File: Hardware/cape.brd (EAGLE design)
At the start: 87 x 118 mm, 67 parts, among them IC1 RT7258, IC2 RT7258, J1 JST-BM07B-GHS-TBT, J10 JST-BM07B-GHS-TBT, J11 JST-BM07B-GHS-TBT, J12 JST-BM07B-GHS-TBT, J13 JST-BM07B-GHS-TBT, J14 JST-BM07B-GHS-TBT, J15 JST-BM07B-GHS-TBT, J16 JST-BM07B-GHS-TBT, J17 JST-BM07B-GHS-TBT, J18 JST-BM07B-GHS-TBT, J19 JST-BM07B-GHS-TBT, J2 JST-BM07B-GHS-TBT, J20 JST-BM07B-GHS-TBT, J21 JST-BM07B-GHS-TBT, J22 JST-BM07B-GHS-TBT, J23 JST-BM07B-GHS-TBT, J24 JST-BM07B-GHS-TBT, J25 JST-BM07B-GHS-TBT, J26 JST-BM07B-GHS-TBT, J27 JST-BM07B-GHS-TBT, J28 JST-BM07B-GHS-TBT, J29 JST-BM07B-GHS-TBT, J3 JST-BM07B-GHS-TBT, J30 JST-BM07B-GHS-TBT, J31 JST-BM07B-GHS-TBT, J32 JST-BM07B-GHS-TBT, J4 JST-BM07B-GHS-TBT, J5 JST-BM07B-GHS-TBT, J6 JST-BM07B-GHS-TBT, J7 JST-BM07B-GHS-TBT, J8 JST-BM07B-GHS-TBT, J9 JST-BM07B-GHS-TBT, Q1 FDS6670, Q2 FDS6670, X1 RJ45-6L2-B, X2 RJ45-6L2-B

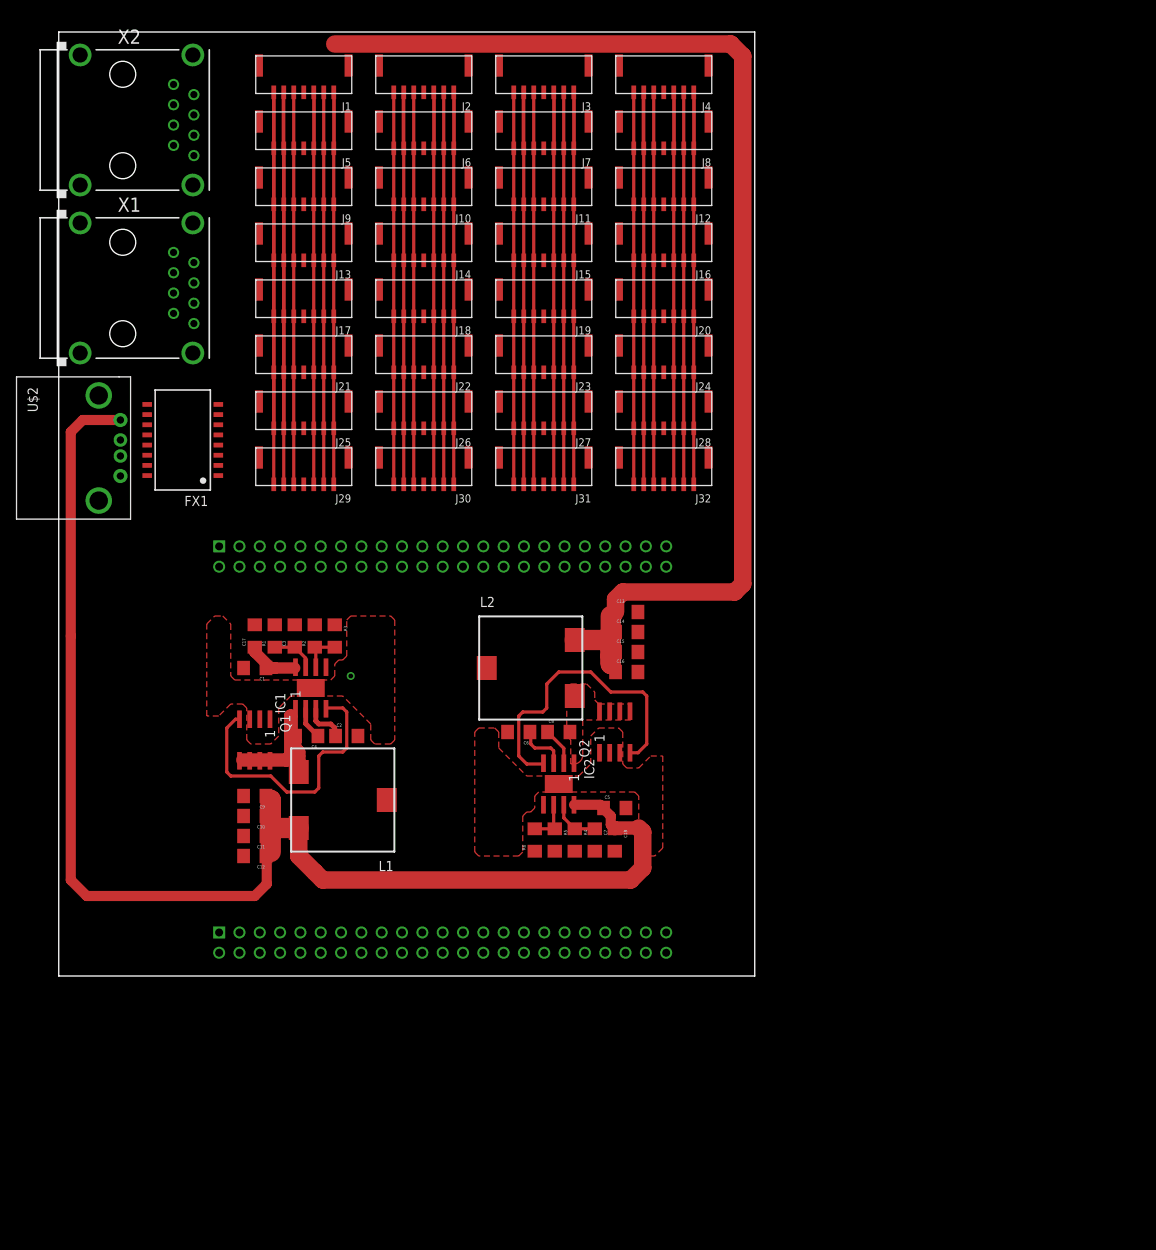
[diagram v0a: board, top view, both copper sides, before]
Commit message: added circuits to control backlights, but I'm going to pull them out for this revision
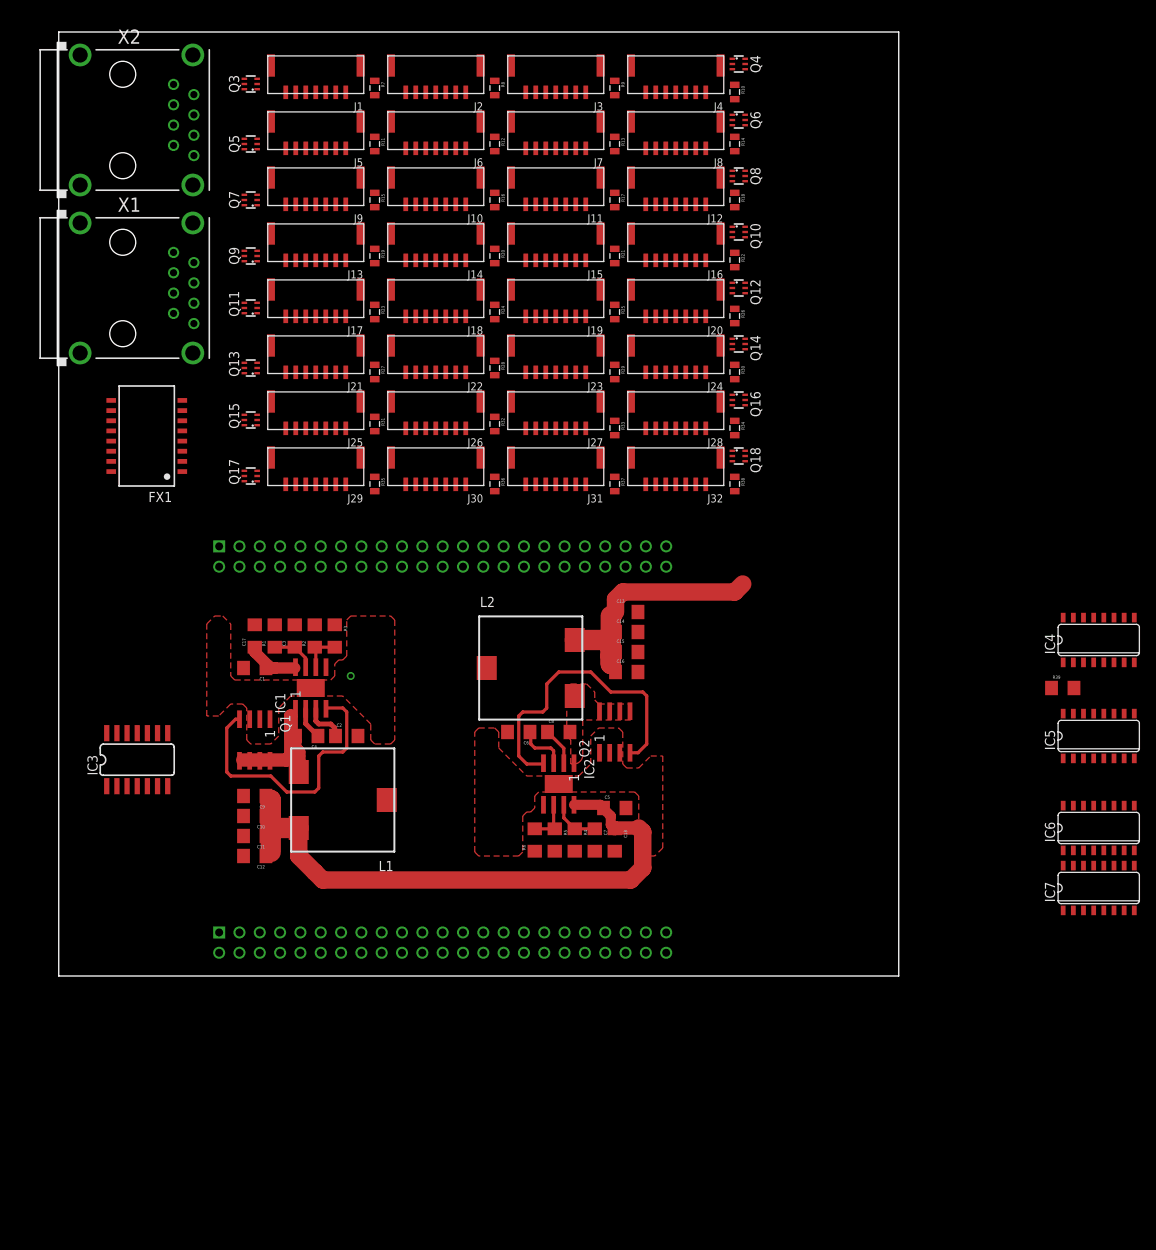
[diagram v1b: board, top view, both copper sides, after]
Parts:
- removed U$2: USBA, Livestream:USB-A-PTH
- added IC3: 74HC125, TotU:SOIC-14
- added IC4, IC5, IC6, IC7: 74LS595D, SparkFun-DigitalIC:SO16
- added Q10, Q11, Q12, Q13, Q14, Q15, Q16, Q17, Q18, Q3, Q4, Q5, Q6, Q7, Q8, Q9: MOSFET-N-DUAL, TotU:SOT-363
- added R10, R11, R12, R13, R14, R15, R16, R17, R18, R19, R20, R21, R22, R23, R24, R25, R26, R27, R28, R29, R30, R31, R32, R33, R34, R35, R36, R37, R38, R7, R8, R9: 12R/0.5W, SparkFun-Resistors:0805
- added R39: 10k, SparkFun-Passives:1206
- moved FX1 4.53 mm to (11.0, 67.5)
- moved J1 1.50 mm to (31.5, 113.0)
- moved J10 1.50 mm to (46.5, 99.0)
- moved J11 1.50 mm to (61.5, 99.0)
- moved J12 1.50 mm to (76.5, 99.0)
- moved J13 1.50 mm to (31.5, 92.0)
- moved J14 1.50 mm to (46.5, 92.0)
- moved J15 1.50 mm to (61.5, 92.0)
- moved J16 1.50 mm to (76.5, 92.0)
- moved J17 1.50 mm to (31.5, 85.0)
- moved J18 1.50 mm to (46.5, 85.0)
- moved J19 1.50 mm to (61.5, 85.0)
- moved J2 1.50 mm to (46.5, 113.0)
- moved J20 1.50 mm to (76.5, 85.0)
- moved J21 1.50 mm to (31.5, 78.0)
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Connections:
- removed net LED: J1.6, J10.6, J11.6, J12.6, J13.6, J14.6, J15.6, J16.6, J17.6, J18.6, J19.6, J2.6, J20.6, J21.6, J22.6, J23.6, J24.6, J25.6, J26.6, J27.6, J28.6, J29.6, J3.6, J30.6, J31.6, J32.6, J4.6, J5.6, J6.6, J7.6, J8.6, J9.6
- removed net SDI-2: J2.4
- new net BL_LATCH: IC4.12, IC5.12, IC6.12, IC7.12
- new net BL_MOSI: IC4.14
- new net BL_OE: IC4.13, IC5.13, IC6.13, IC7.13, R39.1
- new net BL_SCK: IC4.11, IC5.11, IC6.11, IC7.11
- new net DC_RAW: IC3.5
- new net LED-1: J1.7, R7.2
- new net LED-10: J10.7, R16.2
- new net LED-11: J11.7, R17.2
- new net LED-12: J12.7, R18.2
- new net LED-13: J13.7, R19.2
- new net LED-14: J14.7, R20.2
- new net LED-15: J15.7, R21.2
- new net LED-16: J16.7, R22.2
- new net LED-17: J17.7, R23.2
- new net LED-18: J18.7, R24.2
- new net LED-19: J19.7, R25.2
- new net LED-2: J2.7, R8.2
- new net LED-20: J20.7, R26.2
- new net LED-21: J21.7, R27.2
- new net LED-22: J22.7, R28.2
- new net LED-23: J23.7, R29.2
- new net LED-24: J24.7, R30.2
- new net LED-25: J25.7, R31.2
- new net LED-26: J26.7, R32.2
- new net LED-27: J27.7, R33.2
- new net LED-28: J28.7, R34.2
- new net LED-29: J29.7, R35.2
- new net LED-3: J3.7, R9.2
- new net LED-30: J30.7, R36.2
- new net LED-31: J31.7, R37.2
- new net LED-32: J32.7, R38.2
- new net LED-4: J4.7, R10.2
- new net LED-5: J5.7, R11.2
- new net LED-6: J6.7, R12.2
- new net LED-7: J7.7, R13.2
- new net LED-8: J8.7, R14.2
- new net LED-9: J9.7, R15.2
- new net N$13: Q4.3, R10.1
- new net N$16: Q3.6, R7.1
- new net N$17: Q3.3, R8.1
- new net N$18: Q5.6, R11.1
- new net N$19: Q5.3, R12.1
- new net N$20: Q6.6, R13.1
- new net N$21: Q6.3, R14.1
- new net N$22: Q7.6, R15.1
- new net N$23: Q7.3, R16.1
- new net N$24: Q8.6, R17.1
- new net N$25: Q8.3, R18.1
- new net N$26: Q9.6, R19.1
- new net N$27: Q9.3, R20.1
- new net N$28: Q10.6, R21.1
- new net N$29: Q10.3, R22.1
- new net N$30: Q11.6, R23.1
- new net N$31: Q11.3, R24.1
- new net N$32: Q12.6, R25.1
- new net N$33: Q12.3, R26.1
- new net N$34: Q13.6, R27.1
- new net N$35: Q13.3, R28.1
- new net N$36: Q14.6, R29.1
- new net N$37: Q14.3, R30.1
- new net N$38: Q15.6, R31.1
- new net N$39: Q15.3, R32.1
- new net N$40: Q16.6, R33.1
- new net N$41: Q16.3, R34.1
- new net N$42: Q17.6, R35.1
- new net N$43: Q17.3, R36.1
- new net N$44: Q18.6, R37.1
- new net N$45: Q18.3, R38.1
- new net N$46: IC4.9, IC5.14
- new net N$47: IC6.9, IC7.14
- new net N$48: IC5.9, IC6.14
- new net N$5: Q4.6, R9.1
- new net N$6: IC3.12
- new net PWM-1: IC4.15, Q3.2
- new net PWM-10: IC5.1, Q7.5
- new net PWM-11: IC5.2, Q8.2
- new net PWM-12: IC5.3, Q8.5
- new net PWM-13: IC5.4, Q9.2
- new net PWM-14: IC5.5, Q9.5
- new net PWM-15: IC5.6, Q10.2
- new net PWM-16: IC5.7, Q10.5
- new net PWM-17: IC6.15, Q11.2
- new net PWM-18: IC6.1, Q11.5
- new net PWM-19: IC6.2, Q12.2
- new net PWM-2: IC4.1, Q3.5
- new net PWM-20: IC6.3, Q12.5
- new net PWM-21: IC6.4, Q13.2
- new net PWM-22: IC6.5, Q13.5
- new net PWM-23: IC6.6, Q14.2
- new net PWM-24: IC6.7, Q14.5
- new net PWM-25: IC7.15, Q15.2
- new net PWM-26: IC7.1, Q15.5
- new net PWM-27: IC7.2, Q16.2
- new net PWM-28: IC7.3, Q16.5
- new net PWM-29: IC7.4, Q17.2
- new net PWM-3: IC4.2, Q4.2
- new net PWM-30: IC7.5, Q17.5
- new net PWM-31: IC7.6, Q18.2
- new net PWM-32: IC7.7, Q18.5
- new net PWM-4: IC4.3, Q4.5
- new net PWM-5: IC4.4, Q5.2
- new net PWM-6: IC4.5, Q5.5
- new net PWM-7: IC4.6, Q6.2
- new net PWM-8: IC4.7, Q6.5
- new net PWM-9: IC5.15, Q7.2
- new net RST_RAW: IC3.9
- new net SCL_RAW: IC3.2
- net GND: now also IC3.1, IC3.10, IC3.13, IC3.4, IC3.7, IC4.8, IC5.8, IC6.8, IC7.8, J1.4, J10.4, J11.4, J12.4, J13.4, J14.4, J15.4, J16.4, J17.4, J18.4, J19.4, J2.4, J20.4, J21.4, J22.4, J23.4, J24.4, J25.4, J26.4, J27.4, J28.4, J29.4, J3.4, J30.4, J31.4, J32.4, J4.4, J5.4, J6.4, J7.4, J8.4, J9.4, Q10.1, Q10.4, Q11.1, Q11.4, Q12.1, Q12.4, Q13.1, Q13.4, Q14.1, Q14.4, Q15.1, Q15.4, Q16.1, Q16.4, Q17.1, Q17.4, Q18.1, Q18.4, Q3.1, Q3.4, Q4.1, Q4.4, Q5.1, Q5.4, Q6.1, Q6.4, Q7.1, Q7.4, Q8.1, Q8.4, Q9.1, Q9.4; no longer J1.1, J10.1, J11.1, J12.1, J13.1, J14.1, J15.1, J16.1, J17.1, J18.1, J19.1, J2.1, J20.1, J21.1, J22.1, J23.1, J24.1, J25.1, J26.1, J27.1, J28.1, J29.1, J3.1, J30.1, J31.1, J32.1, J4.1, J5.1, J6.1, J7.1, J8.1, J9.1, U$2.GND
- net SDI-1: now also J1.1, J2.1; no longer J1.4
- net SDI-10: now also J10.1; no longer J10.4
- net SDI-11: now also J11.1; no longer J11.4
- net SDI-12: now also J12.1; no longer J12.4
- net SDI-13: now also J13.1; no longer J13.4
- net SDI-14: now also J14.1; no longer J14.4
- net SDI-15: now also J15.1; no longer J15.4
- net SDI-16: now also J16.1; no longer J16.4
- net SDI-17: now also J17.1; no longer J17.4
- net SDI-18: now also J18.1; no longer J18.4
- net SDI-19: now also J19.1; no longer J19.4
- net SDI-20: now also J20.1; no longer J20.4
- net SDI-21: now also J21.1; no longer J21.4
- net SDI-22: now also J22.1; no longer J22.4
- net SDI-23: now also J23.1; no longer J23.4
- net SDI-24: now also J24.1; no longer J24.4
- net SDI-25: now also J25.1; no longer J25.4
- net SDI-26: now also J26.1; no longer J26.4
- net SDI-27: now also J27.1; no longer J27.4
- net SDI-28: now also J28.1; no longer J28.4
- net SDI-29: now also J29.1; no longer J29.4
- net SDI-3: now also J3.1; no longer J3.4
- net SDI-30: now also J30.1; no longer J30.4
- net SDI-31: now also J31.1; no longer J31.4
- net SDI-32: now also J32.1; no longer J32.4
- net SDI-4: now also J4.1; no longer J4.4
- net SDI-5: now also J5.1; no longer J5.4
- net SDI-6: now also J6.1; no longer J6.4
- net SDI-7: now also J7.1; no longer J7.4
- net SDI-8: now also J8.1; no longer J8.4
- net SDI-9: now also J9.1; no longer J9.4
- net VCC3V3: now also IC4.10, IC4.16, IC5.10, IC5.16, IC6.10, IC6.16, IC7.10, IC7.16, J1.6, J10.6, J11.6, J12.6, J13.6, J14.6, J15.6, J16.6, J17.6, J18.6, J19.6, J2.6, J20.6, J21.6, J22.6, J23.6, J24.6, J25.6, J26.6, J27.6, J28.6, J29.6, J3.6, J30.6, J31.6, J32.6, J4.6, J5.6, J6.6, J7.6, J8.6, J9.6, R39.2; no longer J1.7, J10.7, J11.7, J12.7, J13.7, J14.7, J15.7, J16.7, J17.7, J18.7, J19.7, J2.7, J20.7, J21.7, J22.7, J23.7, J24.7, J25.7, J26.7, J27.7, J28.7, J29.7, J3.7, J30.7, J31.7, J32.7, J4.7, J5.7, J6.7, J7.7, J8.7, J9.7
- net VCC5V: now also U$1.51; no longer U$2.VBUS
- net VDD_5V: no longer U$1.51
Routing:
- net VCC3V3: track 518.4 -> 36.2 mm
- net SCL: track 365.1 -> 0.00 mm
- net RST: track 364.7 -> 0.00 mm
- net LED: track 364.0 -> 0.00 mm
- net DC: track 364.0 -> 0.00 mm
- net GND: track 357.0 -> 0.00 mm
- net VCC5V: track 176.4 -> 83.1 mm
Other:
- board size 87 x 118 mm -> 105 x 118 mm

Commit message: removed led drivers, added backlight resistors
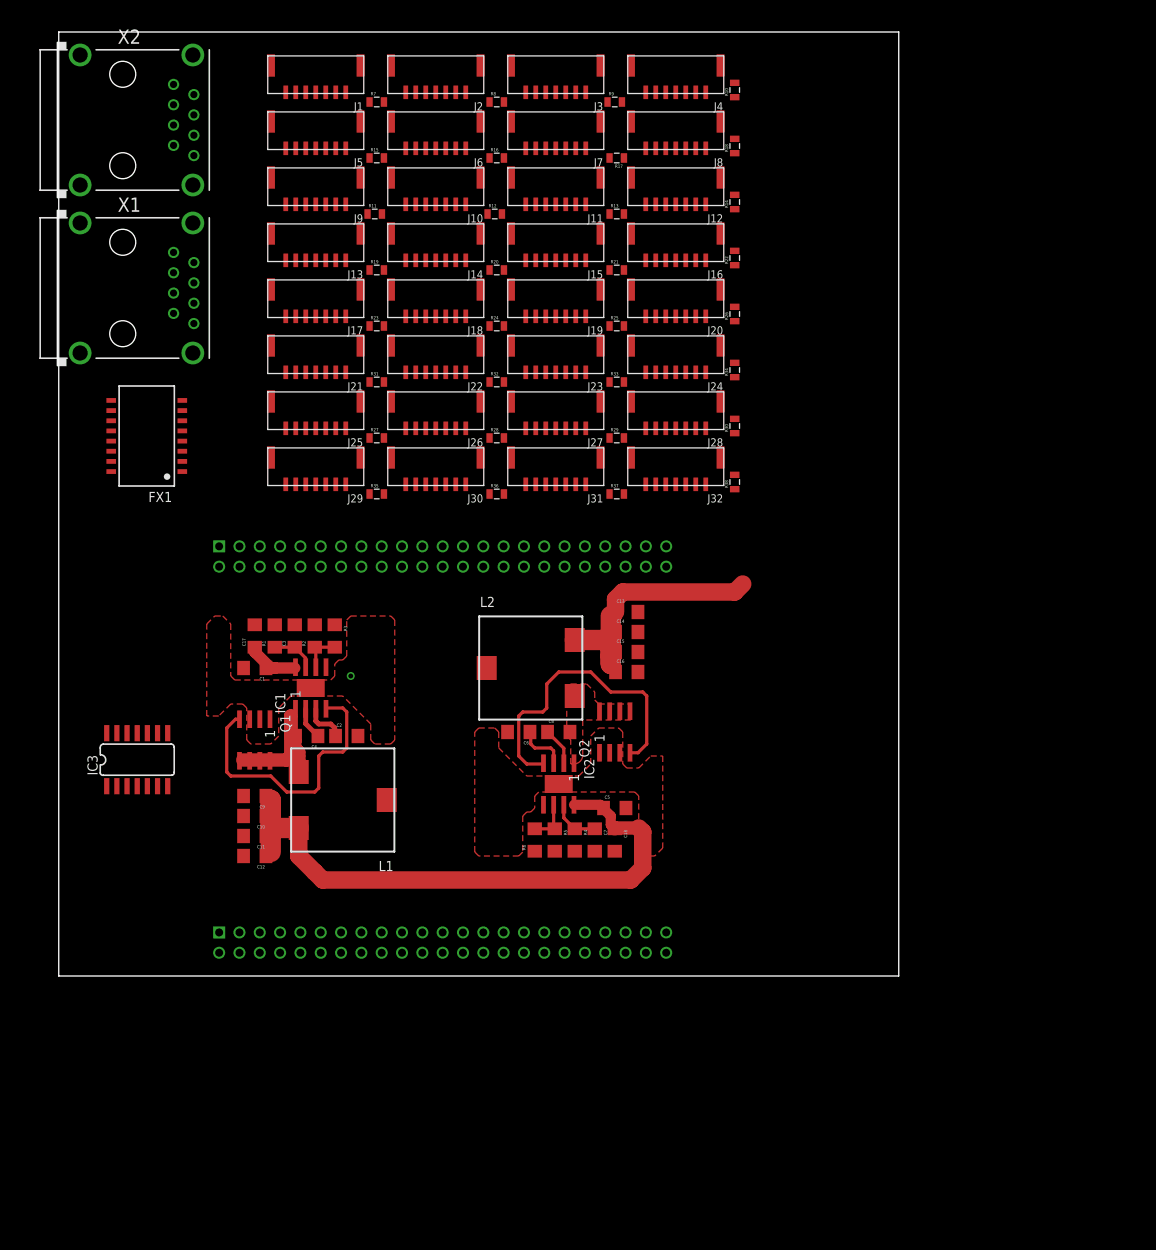
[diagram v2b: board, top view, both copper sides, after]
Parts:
- removed IC4, IC5, IC6, IC7: 74LS595D, SparkFun-DigitalIC:SO16
- removed Q10, Q11, Q12, Q13, Q14, Q15, Q16, Q17, Q18, Q3, Q4, Q5, Q6, Q7, Q8, Q9: MOSFET-N-DUAL, TotU:SOT-363
- removed R39: 10k, SparkFun-Passives:1206
- R10, R11, R12, R13, R14, R15, R16, R17, R18, R19, R20, R21, R22, R23, R24, R25, R26, R27, R28, R29, R30, R31, R32, R33, R34, R35, R36, R37, R38, R7, R8, R9: value 12R/0.5W -> (none); device SparkFun-Resistors:0805 -> SparkFun-Passives:0805
- moved R13 8.75 mm to (69.8, 95.2), turned to 0 degrees
- moved R28 8.75 mm to (54.8, 67.2), turned to 0 degrees
- moved R11 8.75 mm to (39.5, 95.2), turned to 0 degrees
- moved R12 8.75 mm to (54.5, 95.2), turned to 0 degrees
- moved R27 8.25 mm to (39.8, 67.2), turned to 0 degrees
- moved R29 8.25 mm to (69.8, 67.2), turned to 0 degrees
- moved R14 7.25 mm to (84.5, 96.8), turned to 90 degrees
- moved R34 7.25 mm to (84.5, 75.8), turned to 90 degrees
- moved R18 6.75 mm to (84.5, 103.8), turned to 90 degrees
- moved R30 6.75 mm to (84.5, 68.8), turned to 90 degrees
- moved R33 5.76 mm to (69.8, 74.2), turned to 0 degrees
- moved R15 5.26 mm to (39.8, 102.2), turned to 0 degrees
- moved R16 5.26 mm to (54.8, 102.2), turned to 0 degrees
- moved R17 5.26 mm to (69.8, 102.2), turned to 180 degrees
- moved R31 5.26 mm to (39.8, 74.2), turned to 0 degrees
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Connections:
- removed net BL_LATCH: IC4.12, IC5.12, IC6.12, IC7.12
- removed net BL_MOSI: IC4.14
- removed net BL_OE: IC4.13, IC5.13, IC6.13, IC7.13, R39.1
- removed net BL_SCK: IC4.11, IC5.11, IC6.11, IC7.11
- removed net N$13: Q4.3, R10.1
- removed net N$16: Q3.6, R7.1
- removed net N$17: Q3.3, R8.1
- removed net N$18: Q5.6, R11.1
- removed net N$19: Q5.3, R12.1
- removed net N$20: Q6.6, R13.1
- removed net N$21: Q6.3, R14.1
- removed net N$22: Q7.6, R15.1
- removed net N$23: Q7.3, R16.1
- removed net N$24: Q8.6, R17.1
- removed net N$25: Q8.3, R18.1
- removed net N$26: Q9.6, R19.1
- removed net N$27: Q9.3, R20.1
- removed net N$28: Q10.6, R21.1
- removed net N$29: Q10.3, R22.1
- removed net N$30: Q11.6, R23.1
- removed net N$31: Q11.3, R24.1
- removed net N$32: Q12.6, R25.1
- removed net N$33: Q12.3, R26.1
- removed net N$34: Q13.6, R27.1
- removed net N$35: Q13.3, R28.1
- removed net N$36: Q14.6, R29.1
- removed net N$37: Q14.3, R30.1
- removed net N$38: Q15.6, R31.1
- removed net N$39: Q15.3, R32.1
- removed net N$40: Q16.6, R33.1
- removed net N$41: Q16.3, R34.1
- removed net N$42: Q17.6, R35.1
- removed net N$43: Q17.3, R36.1
- removed net N$44: Q18.6, R37.1
- removed net N$45: Q18.3, R38.1
- removed net N$46: IC4.9, IC5.14
- removed net N$47: IC6.9, IC7.14
- removed net N$48: IC5.9, IC6.14
- removed net N$5: Q4.6, R9.1
- removed net PWM-1: IC4.15, Q3.2
- removed net PWM-10: IC5.1, Q7.5
- removed net PWM-11: IC5.2, Q8.2
- removed net PWM-12: IC5.3, Q8.5
- removed net PWM-13: IC5.4, Q9.2
- removed net PWM-14: IC5.5, Q9.5
- removed net PWM-15: IC5.6, Q10.2
- removed net PWM-16: IC5.7, Q10.5
- removed net PWM-17: IC6.15, Q11.2
- removed net PWM-18: IC6.1, Q11.5
- removed net PWM-19: IC6.2, Q12.2
- removed net PWM-2: IC4.1, Q3.5
- removed net PWM-20: IC6.3, Q12.5
- removed net PWM-21: IC6.4, Q13.2
- removed net PWM-22: IC6.5, Q13.5
- removed net PWM-23: IC6.6, Q14.2
- removed net PWM-24: IC6.7, Q14.5
- removed net PWM-25: IC7.15, Q15.2
- removed net PWM-26: IC7.1, Q15.5
- removed net PWM-27: IC7.2, Q16.2
- removed net PWM-28: IC7.3, Q16.5
- removed net PWM-29: IC7.4, Q17.2
- removed net PWM-3: IC4.2, Q4.2
- removed net PWM-30: IC7.5, Q17.5
- removed net PWM-31: IC7.6, Q18.2
- removed net PWM-32: IC7.7, Q18.5
- removed net PWM-4: IC4.3, Q4.5
- removed net PWM-5: IC4.4, Q5.2
- removed net PWM-6: IC4.5, Q5.5
- removed net PWM-7: IC4.6, Q6.2
- removed net PWM-8: IC4.7, Q6.5
- removed net PWM-9: IC5.15, Q7.2
- net GND: no longer IC4.8, IC5.8, IC6.8, IC7.8, Q10.1, Q10.4, Q11.1, Q11.4, Q12.1, Q12.4, Q13.1, Q13.4, Q14.1, Q14.4, Q15.1, Q15.4, Q16.1, Q16.4, Q17.1, Q17.4, Q18.1, Q18.4, Q3.1, Q3.4, Q4.1, Q4.4, Q5.1, Q5.4, Q6.1, Q6.4, Q7.1, Q7.4, Q8.1, Q8.4, Q9.1, Q9.4
- net LED-1: now also R7.1; no longer R7.2
- net LED-10: now also R12.1; no longer R16.2
- net LED-11: now also R13.1; no longer R17.2
- net LED-12: now also R14.1; no longer R18.2
- net LED-13: now also R19.1; no longer R19.2
- net LED-14: now also R20.1; no longer R20.2
- net LED-15: now also R21.1; no longer R21.2
- net LED-16: now also R22.1; no longer R22.2
- net LED-17: now also R23.1; no longer R23.2
- net LED-18: now also R24.1; no longer R24.2
- net LED-19: now also R25.1; no longer R25.2
- net LED-2: now also R8.1; no longer R8.2
- net LED-20: now also R26.1; no longer R26.2
- net LED-21: now also R31.1; no longer R27.2
- net LED-22: now also R32.1; no longer R28.2
- net LED-23: now also R33.1; no longer R29.2
- net LED-24: now also R34.1; no longer R30.2
- net LED-25: now also R27.1; no longer R31.2
- net LED-26: now also R28.1; no longer R32.2
- net LED-27: now also R29.1; no longer R33.2
- net LED-28: now also R30.1; no longer R34.2
- net LED-29: now also R35.1; no longer R35.2
- net LED-3: now also R9.1; no longer R9.2
- net LED-30: now also R36.1; no longer R36.2
- net LED-31: now also R37.1; no longer R37.2
- net LED-32: now also R38.1; no longer R38.2
- net LED-4: now also R10.1; no longer R10.2
- net LED-5: now also R15.1; no longer R11.2
- net LED-6: now also R16.1; no longer R12.2
- net LED-7: now also R17.1; no longer R13.2
- net LED-8: now also R18.1; no longer R14.2
- net LED-9: now also R11.1; no longer R15.2
- net VCC3V3: no longer IC4.10, IC4.16, IC5.10, IC5.16, IC6.10, IC6.16, IC7.10, IC7.16, R39.2
- net VCC5V: now also R10.2, R11.2, R12.2, R13.2, R14.2, R15.2, R16.2, R17.2, R18.2, R19.2, R20.2, R21.2, R22.2, R23.2, R24.2, R25.2, R26.2, R27.2, R28.2, R29.2, R30.2, R31.2, R32.2, R33.2, R34.2, R35.2, R36.2, R37.2, R38.2, R7.2, R8.2, R9.2
